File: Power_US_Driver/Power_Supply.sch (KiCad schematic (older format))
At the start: 6 parts, among them T1 Transformer_1P_1S, U1 LM7805_TO220

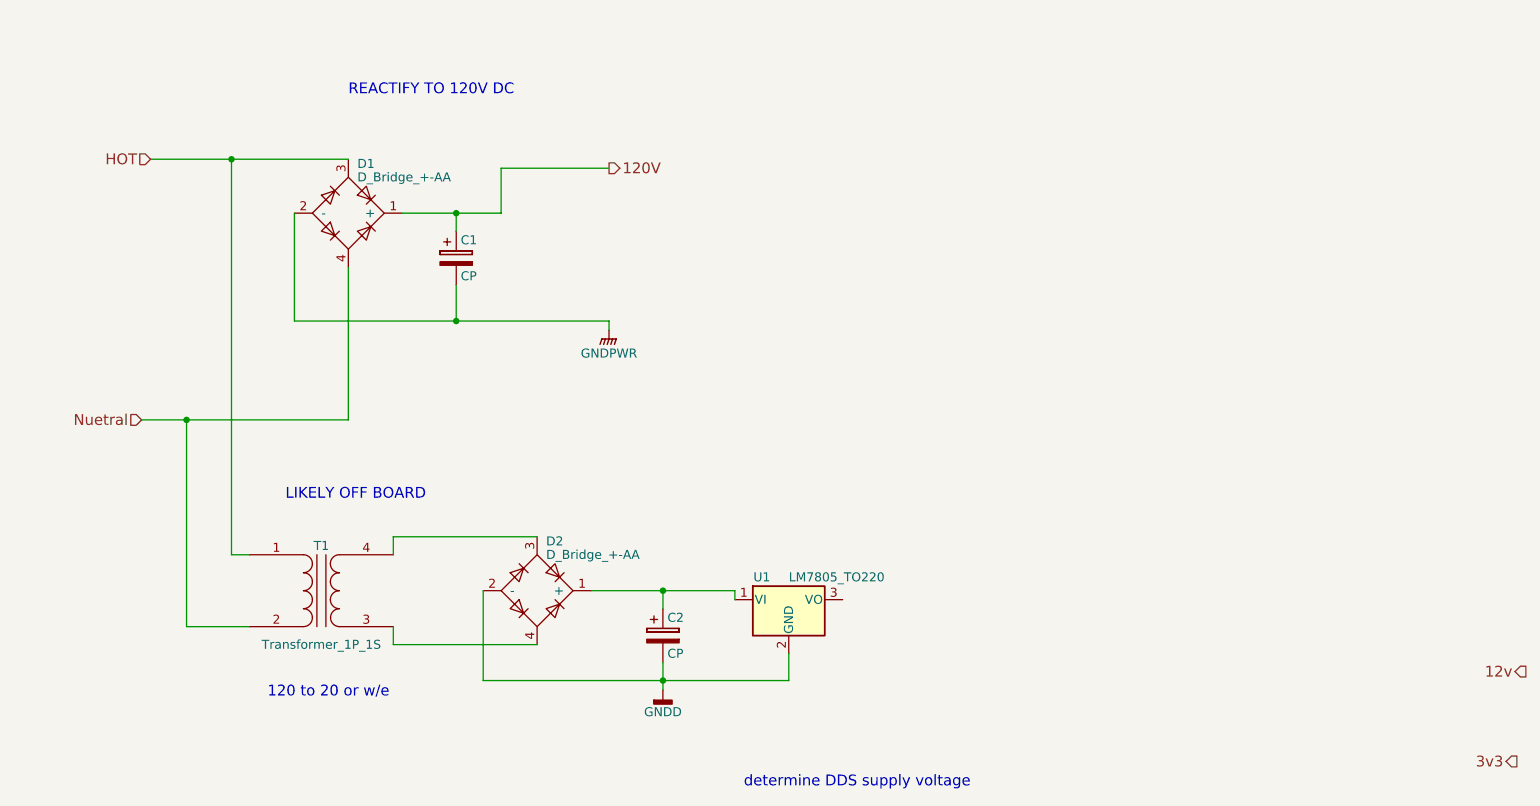
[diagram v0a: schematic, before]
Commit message: CURRENT SENSE REROUT, HIGHSIDE DRIVER GROUNDING
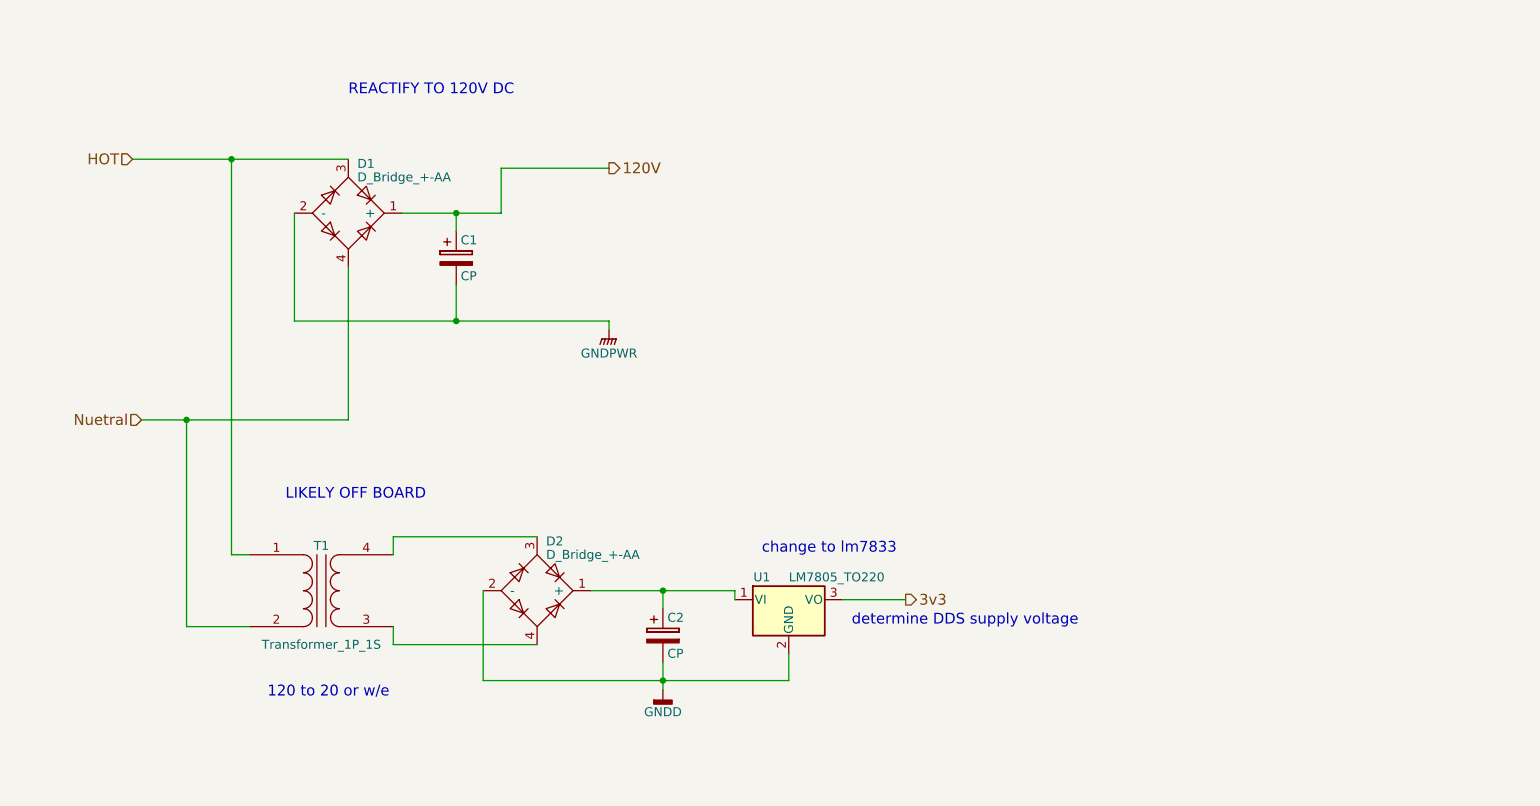
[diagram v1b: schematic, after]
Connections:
- net 3v3: now also U1.3 (VO)
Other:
- note added: "change to lm7833"
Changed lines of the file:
@@
 LIBS:LIA-cache
 LIBS:power_US
+LIBS:JasMoH_Parts
 LIBS:Power_US_Driver-cache
 EELAYER 25 0
@@
 Text HLabel 3700 2050 2    60   Output ~ 0
 120V
-Text HLabel 1150 2000 0    60   Input ~ 0
+Text HLabel 1050 2000 0    60   Input ~ 0
 HOT
 Text HLabel 1100 3450 0    60   Input ~ 0
 Nuetral
-Text HLabel 8800 4850 0    60   Output ~ 0
-12v
-Text HLabel 8750 5350 0    60   Output ~ 0
+Text HLabel 5350 4450 2    60   Output ~ 0
 3v3
 $Comp
@@
 	1    0    0    -1
 $EndComp
-Text Notes 4450 5500 0    60   ~ 0
+Text Notes 5050 4600 0    60   ~ 0
 determine DDS supply voltage
 Wire Wire Line
-	1150 2000 1600 2000
-Wire Wire Line
-	1600 2000 2250 2000
+	1050 2000 2250 2000
 Wire Wire Line
 	2250 3450 2250 2600
 Wire Wire Line
-	1100 3450 1350 3450
+	1100 3450 2250 3450
 Wire Wire Line
-	1350 3450 2250 3450
-Wire Wire Line
-	2550 2300 2850 2300
-Wire Wire Line
-	2850 2300 3100 2300
+	2550 2300 3100 2300
 Wire Wire Line
 	3100 2300 3100 2050
@@
 	1950 2300 1950 2900
 Wire Wire Line
-	1950 2900 2850 2900
-Wire Wire Line
-	2850 2900 3700 2900
+	1950 2900 3700 2900
 Wire Wire Line
 	1700 4200 1600 4200
@@
 	3000 4400 3000 4900
 Wire Wire Line
-	3000 4900 4000 4900
+	3000 4900 4700 4900
 Wire Wire Line
-	4000 4900 4700 4900
-Wire Wire Line
-	3600 4400 4000 4400
-Wire Wire Line
-	4000 4400 4400 4400
+	3600 4400 4400 4400
 Wire Wire Line
 	4400 4400 4400 4450
@@
 Connection ~ 4000 4400
 Wire Wire Line
-	4000 4800 4000 4900
-Wire Wire Line
-	4000 4900 4000 4950
+	4000 4800 4000 4950
 Connection ~ 4000 4900
 $Comp
-L GNDPWR #PWR?
+L GNDPWR #PWR2
 U 1 1 5AB00CEA
 P 3700 2950
-F 0 "#PWR?" H 3700 2750 50  0001 C CNN
+F 0 "#PWR2" H 3700 2750 50  0001 C CNN
 F 1 "GNDPWR" H 3700 2820 50  0000 C CNN
 F 2 "" H 3700 2900 50  0001 C CNN
@@
 	3700 2900 3700 2950
 $Comp
-L GNDD #PWR?
+L GNDD #PWR3
 U 1 1 5AB013C1
 P 4000 4950
-F 0 "#PWR?" H 4000 4700 50  0001 C CNN
+F 0 "#PWR3" H 4000 4700 50  0001 C CNN
 F 1 "GNDD" H 4000 4825 50  0000 C CNN
 F 2 "" H 4000 4950 50  0001 C CNN
@@
 	1    0    0    -1
 $EndComp
+Wire Wire Line
+	5350 4450 5000 4450
+Text Notes 4550 4200 0    60   ~ 0
+change to lm7833
 $EndSCHEMATC

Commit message: initial Current sense more vacilating over power drive solution
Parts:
- removed D1: D_Bridge_+-AA, symbol D_Bridge_+-AA
- added C7: CP, symbol CP
- added D1, D4: D, symbol D
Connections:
- net GNDPWR: now also C7.1
- net HOT: now also D1.2 (A), D4.1 (K)
- net 120V: no longer names the net of C1.1
- new net V+: D1.1 (K)
- new net V-: C7.2, D4.2 (A)
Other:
- note added: "dimmer circuit for PWR CTL?"
- moved on the sheet: C1
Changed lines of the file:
@@
 120 to 20 or w/e
-$Comp
-L D_Bridge_+-AA D1
-U 1 1 5AAD8E46
-P 2250 2300
-F 0 "D1" H 2300 2575 50  0000 L CNN
-F 1 "D_Bridge_+-AA" H 2300 2500 50  0000 L CNN
-F 2 "" H 2250 2300 50  0001 C CNN
-F 3 "" H 2250 2300 50  0001 C CNN
-	1    2250 2300
-	1    0    0    -1
-$EndComp
 $Comp
 L D_Bridge_+-AA D2
@@
 	1    0    0    -1
 $EndComp
-Text HLabel 3700 2050 2    60   Output ~ 0
-120V
+Text HLabel 3700 2000 2    60   Output ~ 0
+V+
 Text HLabel 1050 2000 0    60   Input ~ 0
 HOT
@@
 Wire Wire Line
 	1050 2000 2250 2000
-Wire Wire Line
-	2250 3450 2250 2600
-Wire Wire Line
-	1100 3450 2250 3450
-Wire Wire Line
-	2550 2300 3100 2300
-Wire Wire Line
-	3100 2300 3100 2050
-Wire Wire Line
-	3100 2050 3700 2050
-Wire Wire Line
-	1950 2300 1950 2900
-Wire Wire Line
-	1950 2900 3700 2900
 Wire Wire Line
 	1700 4200 1600 4200
@@
 L CP C1
 U 1 1 5AAE86CA
-P 2850 2550
-F 0 "C1" H 2875 2650 50  0000 L CNN
-F 1 "CP" H 2875 2450 50  0000 L CNN
-F 2 "" H 2888 2400 50  0001 C CNN
-F 3 "" H 2850 2550 50  0001 C CNN
-	1    2850 2550
+P 2950 2150
+F 0 "C1" H 2975 2250 50  0000 L CNN
+F 1 "CP" H 2975 2050 50  0000 L CNN
+F 2 "" H 2988 2000 50  0001 C CNN
+F 3 "" H 2950 2150 50  0001 C CNN
+	1    2950 2150
 	1    0    0    -1
 $EndComp
-Wire Wire Line
-	2850 2400 2850 2300
-Connection ~ 2850 2300
-Wire Wire Line
-	2850 2700 2850 2900
-Connection ~ 2850 2900
 $Comp
 L CP C2
@@
 Connection ~ 4000 4900
 $Comp
-L GNDPWR #PWR2
+L GNDPWR #PWR4
 U 1 1 5AB00CEA
-P 3700 2950
-F 0 "#PWR2" H 3700 2750 50  0001 C CNN
-F 1 "GNDPWR" H 3700 2820 50  0000 C CNN
-F 2 "" H 3700 2900 50  0001 C CNN
-F 3 "" H 3700 2900 50  0001 C CNN
-	1    3700 2950
+P 3400 2450
+F 0 "#PWR4" H 3400 2250 50  0001 C CNN
+F 1 "GNDPWR" H 3400 2320 50  0000 C CNN
+F 2 "" H 3400 2400 50  0001 C CNN
+F 3 "" H 3400 2400 50  0001 C CNN
+	1    3400 2450
 	1    0    0    -1
 $EndComp
-Wire Wire Line
-	3700 2900 3700 2950
 $Comp
-L GNDD #PWR3
+L GNDD #PWR5
 U 1 1 5AB013C1
 P 4000 4950
-F 0 "#PWR3" H 4000 4700 50  0001 C CNN
+F 0 "#PWR5" H 4000 4700 50  0001 C CNN
 F 1 "GNDD" H 4000 4825 50  0000 C CNN
 F 2 "" H 4000 4950 50  0001 C CNN
@@
 Text Notes 4550 4200 0    60   ~ 0
 change to lm7833
+$Comp
+L D D1
+U 1 1 5AB252E8
+P 2400 2000
+F 0 "D1" H 2400 2100 50  0000 C CNN
+F 1 "D" H 2400 1900 50  0000 C CNN
+F 2 "" H 2400 2000 50  0001 C CNN
+F 3 "" H 2400 2000 50  0001 C CNN
+	1    2400 2000
+	-1   0    0    1
+$EndComp
+$Comp
+L D D4
+U 1 1 5AB2532E
+P 2400 2900
+F 0 "D4" H 2400 3000 50  0000 C CNN
+F 1 "D" H 2400 2800 50  0000 C CNN
+F 2 "" H 2400 2900 50  0001 C CNN
+F 3 "" H 2400 2900 50  0001 C CNN
+	1    2400 2900
+	1    0    0    -1
+$EndComp
+Text HLabel 3700 2900 2    60   Output ~ 0
+V-
+Wire Wire Line
+	3700 2000 2550 2000
+$Comp
+L CP C7
+U 1 1 5AB2577F
+P 2950 2600
+F 0 "C7" H 2975 2700 50  0000 L CNN
+F 1 "CP" H 2975 2500 50  0000 L CNN
+F 2 "" H 2988 2450 50  0001 C CNN
+F 3 "" H 2950 2600 50  0001 C CNN
+	1    2950 2600
+	1    0    0    -1
+$EndComp
+Wire Wire Line
+	2950 2300 2950 2450
+Wire Wire Line
+	2950 2750 2950 2900
+Wire Wire Line
+	2550 2900 3700 2900
+Wire Wire Line
+	3400 2450 3400 2350
+Wire Wire Line
+	3400 2350 2950 2350
+Connection ~ 2950 2350
+Connection ~ 2950 2900
+Wire Wire Line
+	1600 2900 2250 2900
+Connection ~ 2000 3450
+Wire Wire Line
+	2000 3450 1100 3450
+Connection ~ 1600 2900
+Text Notes 2750 1900 0    60   ~ 0
+dimmer circuit for PWR CTL?
 $EndSCHEMATC

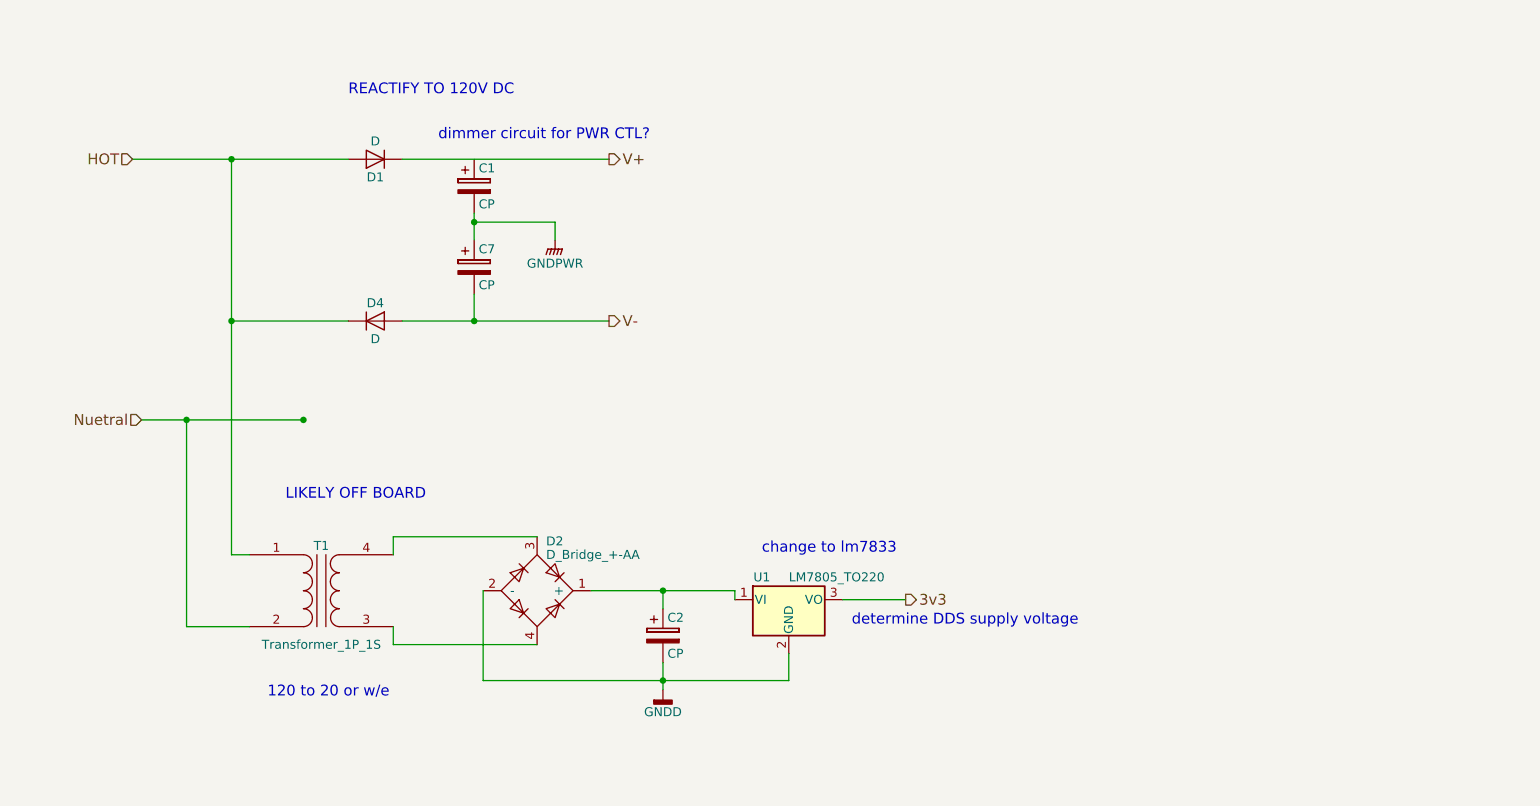
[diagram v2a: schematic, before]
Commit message: Screw it, 0-120V output voltage is fine for a cheapo first pass
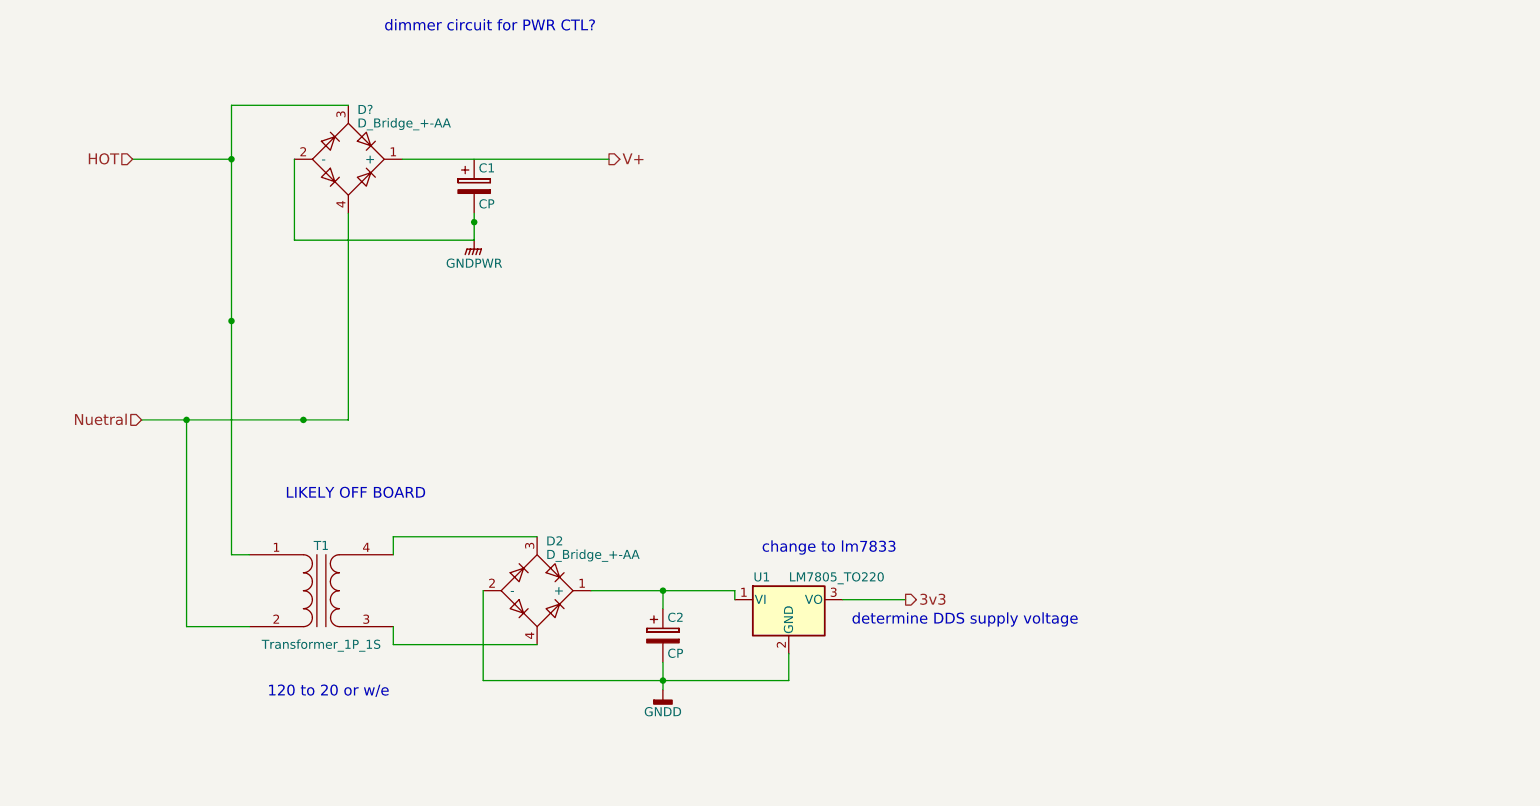
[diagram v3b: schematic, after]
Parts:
- removed C7: CP, symbol CP
- removed D1, D4: D, symbol D
- added D?: D_Bridge_+-AA, symbol D_Bridge_+-AA
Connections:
- net GNDPWR: now also D?.2 (-)
- net HOT: now also D?.3
- net Nuetral: now also D?.4
- net V+: now also D?.1 (+)
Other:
- note removed: "REACTIFY TO 120V DC"
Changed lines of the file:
@@
 determine DDS supply voltage
 Wire Wire Line
-	1050 2000 2250 2000
+	1600 4200 1700 4200
 Wire Wire Line
-	1700 4200 1600 4200
-Wire Wire Line
-	1600 4200 1600 2000
+	1600 1700 1600 4200
 Connection ~ 1600 2000
 Wire Wire Line
@@
 Wire Wire Line
 	4700 4900 4700 4750
-Text Notes 2250 1650 0    60   ~ 0
-REACTIFY TO 120V DC
 Text Notes 1900 3900 0    60   ~ 0
 LIKELY OFF BOARD
@@
 L GNDPWR #PWR4
 U 1 1 5AB00CEA
-P 3400 2450
-F 0 "#PWR4" H 3400 2250 50  0001 C CNN
-F 1 "GNDPWR" H 3400 2320 50  0000 C CNN
-F 2 "" H 3400 2400 50  0001 C CNN
-F 3 "" H 3400 2400 50  0001 C CNN
-	1    3400 2450
+P 2950 2450
+F 0 "#PWR4" H 2950 2250 50  0001 C CNN
+F 1 "GNDPWR" H 2950 2320 50  0000 C CNN
+F 2 "" H 2950 2400 50  0001 C CNN
+F 3 "" H 2950 2400 50  0001 C CNN
+	1    2950 2450
 	1    0    0    -1
 $EndComp
@@
 Text Notes 4550 4200 0    60   ~ 0
 change to lm7833
-$Comp
-L D D1
-U 1 1 5AB252E8
-P 2400 2000
-F 0 "D1" H 2400 2100 50  0000 C CNN
-F 1 "D" H 2400 1900 50  0000 C CNN
-F 2 "" H 2400 2000 50  0001 C CNN
-F 3 "" H 2400 2000 50  0001 C CNN
-	1    2400 2000
-	-1   0    0    1
-$EndComp
-$Comp
-L D D4
-U 1 1 5AB2532E
-P 2400 2900
-F 0 "D4" H 2400 3000 50  0000 C CNN
-F 1 "D" H 2400 2800 50  0000 C CNN
-F 2 "" H 2400 2900 50  0001 C CNN
-F 3 "" H 2400 2900 50  0001 C CNN
-	1    2400 2900
-	1    0    0    -1
-$EndComp
-Text HLabel 3700 2900 2    60   Output ~ 0
-V-
 Wire Wire Line
 	3700 2000 2550 2000
+Wire Wire Line
+	2950 2300 2950 2450
+Connection ~ 2950 2350
+Connection ~ 2000 3450
+Wire Wire Line
+	1100 3450 2250 3450
+Connection ~ 1600 2900
+Text Notes 2450 1300 0    60   ~ 0
+dimmer circuit for PWR CTL?
 $Comp
-L CP C7
-U 1 1 5AB2577F
-P 2950 2600
-F 0 "C7" H 2975 2700 50  0000 L CNN
-F 1 "CP" H 2975 2500 50  0000 L CNN
-F 2 "" H 2988 2450 50  0001 C CNN
-F 3 "" H 2950 2600 50  0001 C CNN
-	1    2950 2600
+L D_Bridge_+-AA D?
+U 1 1 5AB2B456
+P 2250 2000
+F 0 "D?" H 2300 2275 50  0000 L CNN
+F 1 "D_Bridge_+-AA" H 2300 2200 50  0000 L CNN
+F 2 "" H 2250 2000 50  0001 C CNN
+F 3 "" H 2250 2000 50  0001 C CNN
+	1    2250 2000
 	1    0    0    -1
 $EndComp
 Wire Wire Line
-	2950 2300 2950 2450
+	1950 2000 1950 2450
 Wire Wire Line
-	2950 2750 2950 2900
+	1950 2450 2950 2450
 Wire Wire Line
-	2550 2900 3700 2900
+	2250 3450 2250 2300
 Wire Wire Line
-	3400 2450 3400 2350
+	2250 1700 1600 1700
 Wire Wire Line
-	3400 2350 2950 2350
-Connection ~ 2950 2350
-Connection ~ 2950 2900
-Wire Wire Line
-	1600 2900 2250 2900
-Connection ~ 2000 3450
-Wire Wire Line
-	2000 3450 1100 3450
-Connection ~ 1600 2900
-Text Notes 2750 1900 0    60   ~ 0
-dimmer circuit for PWR CTL?
+	1050 2000 1600 2000
 $EndSCHEMATC
